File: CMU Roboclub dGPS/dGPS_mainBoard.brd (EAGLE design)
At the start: 95.3 x 74.9 mm, 9 parts, among them IC1 LM2937

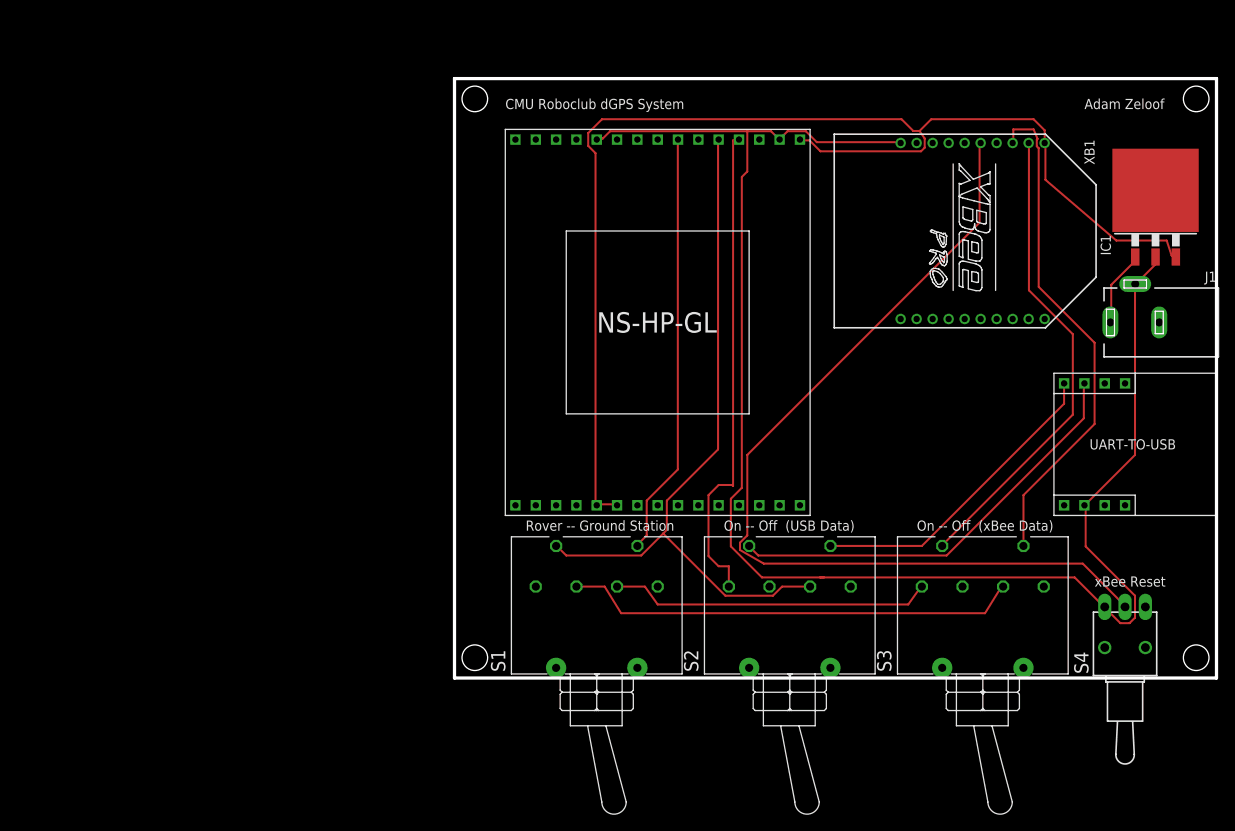
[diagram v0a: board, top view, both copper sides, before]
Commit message: Added decoupling caps, updated board layout
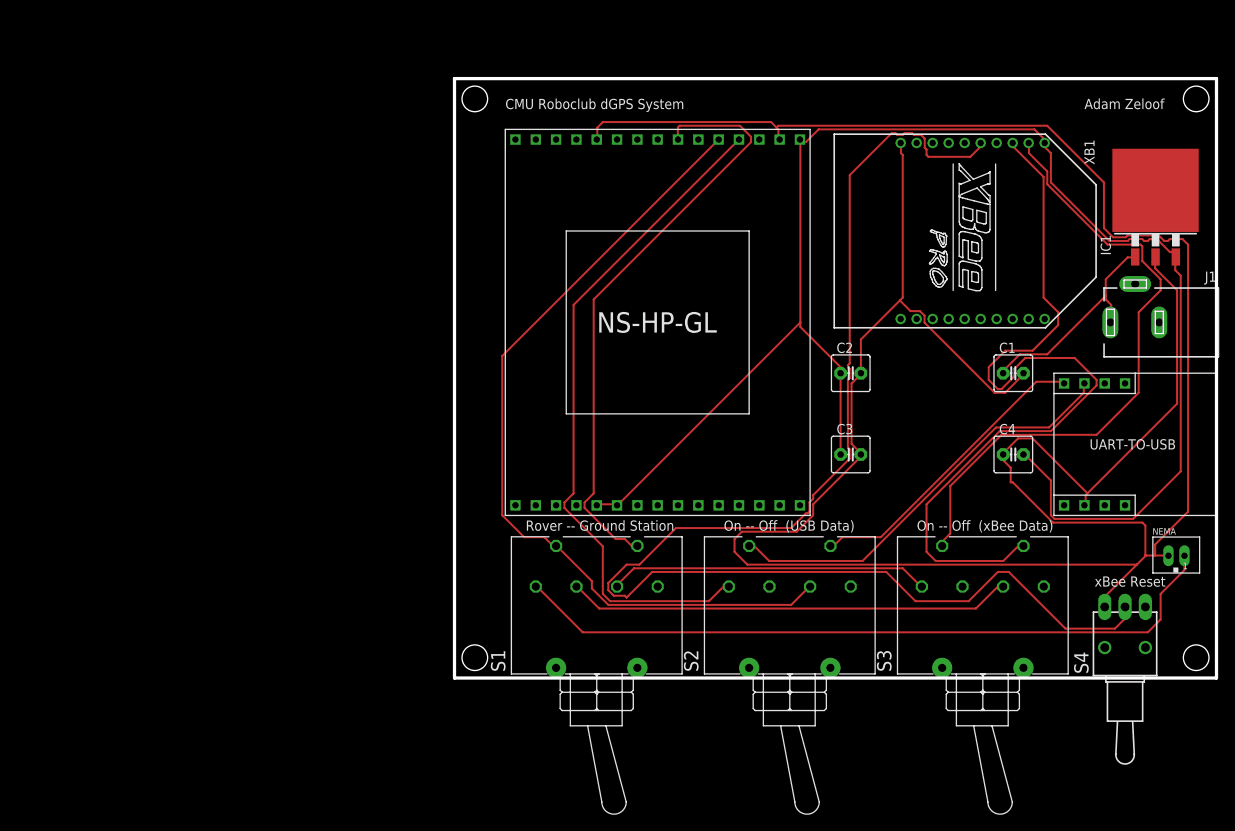
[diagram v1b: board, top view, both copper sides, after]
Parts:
- added C1, C2, C3: 100nF, capacitor-wima:C2.5-5
- added C4: 1uF, capacitor-wima:C2.5-5
- added NEMA: JST-PH_2-PIN_HEADER, SRG:JST_B2B-PH_HEADER
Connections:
- net N$1: now also C2.1, C3.1, C4.2
- net N$12: now also C1.2, C2.2, C3.2, C4.1, NEMA.P2
- net N$14: now also C1.1
- net N$7: now also NEMA.P1
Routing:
- net N$12: track 199.5 -> 356.0 mm
- net N$7: track 0.00 -> 90.3 mm
- net N$13: track 114.5 -> 170.5 mm
- net N$10: track 63.2 -> 102.3 mm
- net N$1: track 154.9 -> 189.5 mm
- net N$4: track 61.0 -> 84.8 mm
- net N$3: track 52.9 -> 74.9 mm
- net N$11: track 59.4 -> 77.9 mm
- net N$14: track 9.45 -> 27.5 mm
- net N$9: track 89.2 -> 103.0 mm
- net N$6: track 57.0 -> 55.6 mm
- net N$8: track 53.9 -> 52.6 mm
- net N$2: track 39.2 -> 37.9 mm

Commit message: Changed several things
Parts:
- removed U$2: VENUS822A, skytraq:UART-TO-USB
- added S5: Mode Sel., switch:320-938
- added SV1: FTDI, con-lstb:MA06-1
- S1: value Mode Select -> xBee RST; device switch:316-923 -> switch:TL3XYO
- S2: value USB Data -> PWR SEL; device switch:316-923 -> switch:TL3XPO
- S3: value xBee Data -> FTDI Data; device switch:316-923 -> switch:320-938
- S4: value TL32WO -> xBee Data; device switch:TL3XWO -> switch:320-938
- moved S1 70.9 mm to (142.9, 8.89), turned to 270 degrees
- moved S4 46.0 mm to (92.7, 8.89), turned to 270 degrees
- moved S2 35.1 mm to (130.8, 8.89), turned to 270 degrees
- moved NEMA 16.7 mm to (147.3, 31.8), turned to 90 degrees
- moved S3 9.92 mm to (114.3, 8.89), turned to 270 degrees
- moved J1 1.27 mm to (139.7, 43.2)
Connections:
- new net N$15: C1.1, IC1.1, S2.2
- new net N$16: S2.3, SV1.3
- net N$10: now also S4.5; no longer S3.5
- net N$11: now also S4.2; no longer S3.2
- net N$12: now also S1.3, SV1.1; no longer S4.3, U$2.2
- net N$13: now also S1.2; no longer S4.2
- net N$14: now also S2.1; no longer C1.1, IC1.1
- net N$2: now also S3.5, SV1.5; no longer S2.5, U$2.5
- net N$3: now also S5.5; no longer S1.5
- net N$4: now also S3.1; no longer S2.1
- net N$5: now also S4.1, S5.4; no longer S1.4, S3.1
- net N$6: now also S4.4, S5.3; no longer S1.3, S3.4
- net N$7: now also S5.1; no longer S1.1
- net N$8: now also S3.2, SV1.4; no longer S2.2, U$2.6
- net N$9: now also S3.4, S5.2; no longer S1.2, S2.4
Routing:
- net N$12: track 356.0 -> 0.00 mm
- net N$1: track 189.5 -> 0.00 mm
- net N$13: track 170.5 -> 0.00 mm
- net N$9: track 103.0 -> 0.00 mm
- net N$10: track 102.3 -> 0.00 mm
- net N$7: track 90.3 -> 0.00 mm
- net N$4: track 84.8 -> 0.00 mm
- net N$11: track 77.9 -> 0.00 mm
- net N$3: track 74.9 -> 0.00 mm
- net N$6: track 55.6 -> 0.00 mm
- net N$8: track 52.6 -> 0.00 mm
- net N$5: track 40.1 -> 0.00 mm
- net N$2: track 37.9 -> 0.00 mm
- net N$14: track 27.5 -> 0.00 mm
- removed copper zone on layer 1, net GND
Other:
- board text added: "EXT"
- board text added: "FTDI"
- board text added: "GND"
- board text added: "On ----- Off"
- board text removed: "On -- Off (USB Data)"
- board text removed: "On -- Off (xBee Data)"
- board text removed: "xBee Reset"

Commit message: Changed many things
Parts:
- moved C1 117.7 mm to (7.62, 24.1)
- moved SV1 97.8 mm to (54.6, 71.1)
- moved IC1 93.7 mm to (52.1, 33.0)
- moved C2 87.5 mm to (17.8, 24.1)
- moved C4 86.4 mm to (38.1, 24.1)
- moved C3 76.3 mm to (27.9, 24.1)
- moved S1 73.2 mm to (71.1, 23.5)
- moved NEMA 67.2 mm to (80.6, 23.5)
- moved U$1 66.9 mm to (41.9, 30.5), turned to 0 degrees
- moved J1 66.5 mm to (73.7, 35.6)
- moved XB1 54.6 mm to (64.8, 54.6)
- moved S2 54.6 mm to (76.2, 8.89)
- moved S3 54.6 mm to (59.7, 8.89)
- moved S5 54.6 mm to (16.5, 8.89)
- moved S4 54.6 mm to (38.1, 8.89)
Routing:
- net N$12: track 0.00 -> 190.4 mm, vias 0 -> 1
- net N$1: track 0.00 -> 144.0 mm
- net N$15: track 0.00 -> 111.6 mm
- net N$9: track 0.00 -> 105.2 mm
- net N$10: track 0.00 -> 101.1 mm
- net N$11: track 0.00 -> 88.4 mm
- net N$16: track 0.00 -> 85.4 mm, vias 0 -> 1
- net N$2: track 0.00 -> 70.0 mm
- net N$7: track 0.00 -> 67.2 mm
- net N$8: track 0.00 -> 63.4 mm
- net N$3: track 0.00 -> 50.5 mm
- net N$13: track 0.00 -> 44.4 mm
- net N$4: track 0.00 -> 37.6 mm
- net N$6: track 0.00 -> 31.6 mm
- net N$14: track 0.00 -> 26.5 mm
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- added copper zone on layer 1, net N$17
- added copper zone on layer 16, net N$18
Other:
- board size 95.3 x 74.9 mm -> 83.8 x 74.9 mm
- board text added: "FTDI Data"
- board text added: "Mode Sel."
- board text added: "On --- Off"
- board text added: "PWR Sel."
- board text added: "Rover -- GS"
- board text added: "xBee Data"
- board text added: "xBee RST"
- board text removed: "On ----- Off"
- board text removed: "Rover -- Ground Station"

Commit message: Added indicator LEDs and did other stuff
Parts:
- removed IC1: LM2937, linear:TO263-3
- removed J1: (no value), con-jack:DCJ0303
- added LED1: PWR, SRG:JST_B2B-PH_HEADER
- added LED2: xBee Assoc., SRG:JST_B2B-PH_HEADER
- added LED3: xBee RX, SRG:JST_B2B-PH_HEADER
- added LED4: xBee TX, SRG:JST_B2B-PH_HEADER
- added LED5: xBee RX Strength, SRG:JST_B2B-PH_HEADER
- added PWR: (no value), SRG:JST_B2B-PH_HEADER
- added R1, R2, R3, R4, R5: 1k, rcl:0204/5
- added U$2: LD1117V33, LD1117V33:LD1117V33
- moved S1 29.0 mm to (99.1, 31.1)
- moved C1 25.0 mm to (30.5, 34.3)
- moved C2 25.0 mm to (40.6, 34.3)
- moved C4 25.0 mm to (61.0, 34.3)
- moved C3 25.0 mm to (50.8, 34.3)
- moved U$1 24.5 mm to (64.8, 39.4)
- moved NEMA 24.5 mm to (95.2, 43.2)
- moved SV1 24.1 mm to (77.5, 78.7)
- moved XB1 24.1 mm to (87.6, 62.2)
- moved S2 23.2 mm to (99.1, 12.7)
- moved S3 23.2 mm to (82.5, 12.7)
- moved S4 23.2 mm to (61.0, 12.7)
- moved S5 23.2 mm to (39.4, 12.7)
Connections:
- new net N$17: C1.2, C2.2, C3.2, C4.1, LED1.P2, LED2.P2, LED3.P2, LED4.P2, LED5.P2, NEMA.P2, PWR.P2, S1.3, SV1.1, U$1.11, U$1.2, U$2.GND, XB1.10
- new net N$18: R5.1, XB1.6
- new net N$19: LED1.P1, R1.2
- new net N$20: LED2.P1, R2.2
- new net N$21: LED3.P1, R3.2
- new net N$22: LED4.P1, R4.2
- new net N$23: LED5.P1, R5.2
- net N$1: now also R1.1, U$2.OUT; no longer IC1.3
- net N$10: now also R4.1
- net N$11: now also R3.1
- net N$12: now also R2.1, XB1.15; no longer C1.2, C2.2, C3.2, C4.1, IC1.2, J1.2, NEMA.P2, S1.3, SV1.1, U$1.11, U$1.2, XB1.10
- net N$14: now also PWR.P1; no longer J1.1
- net N$15: now also U$2.IN; no longer IC1.1
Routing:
- net N$17: track 0.00 -> 198.1 mm
- net N$12: track 190.4 -> 65.4 mm, vias 1 -> 0
- net N$18: track 0.00 -> 56.2 mm
- net N$11: track 88.4 -> 133.7 mm
- net N$1: track 144.0 -> 171.6 mm
- net N$8: track 63.4 -> 90.1 mm, vias 0 -> 1
- net N$2: track 70.0 -> 87.7 mm
- net N$10: track 101.1 -> 114.7 mm
- net N$16: track 85.4 -> 95.0 mm, vias 1 -> 0
- net N$9: track 105.2 -> 97.8 mm
- net N$13: track 44.4 -> 50.5 mm
- net N$19: track 0.00 -> 5.71 mm
- net N$22: track 0.00 -> 5.71 mm
- net N$23: track 0.00 -> 5.68 mm
- net N$20: track 0.00 -> 5.68 mm
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- removed copper zone on layer 1, net N$17
- removed copper zone on layer 16, net N$18
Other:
- board size 83.8 x 74.9 mm -> 83.8 x 78.7 mm
